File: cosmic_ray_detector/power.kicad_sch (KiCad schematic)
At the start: 16 parts

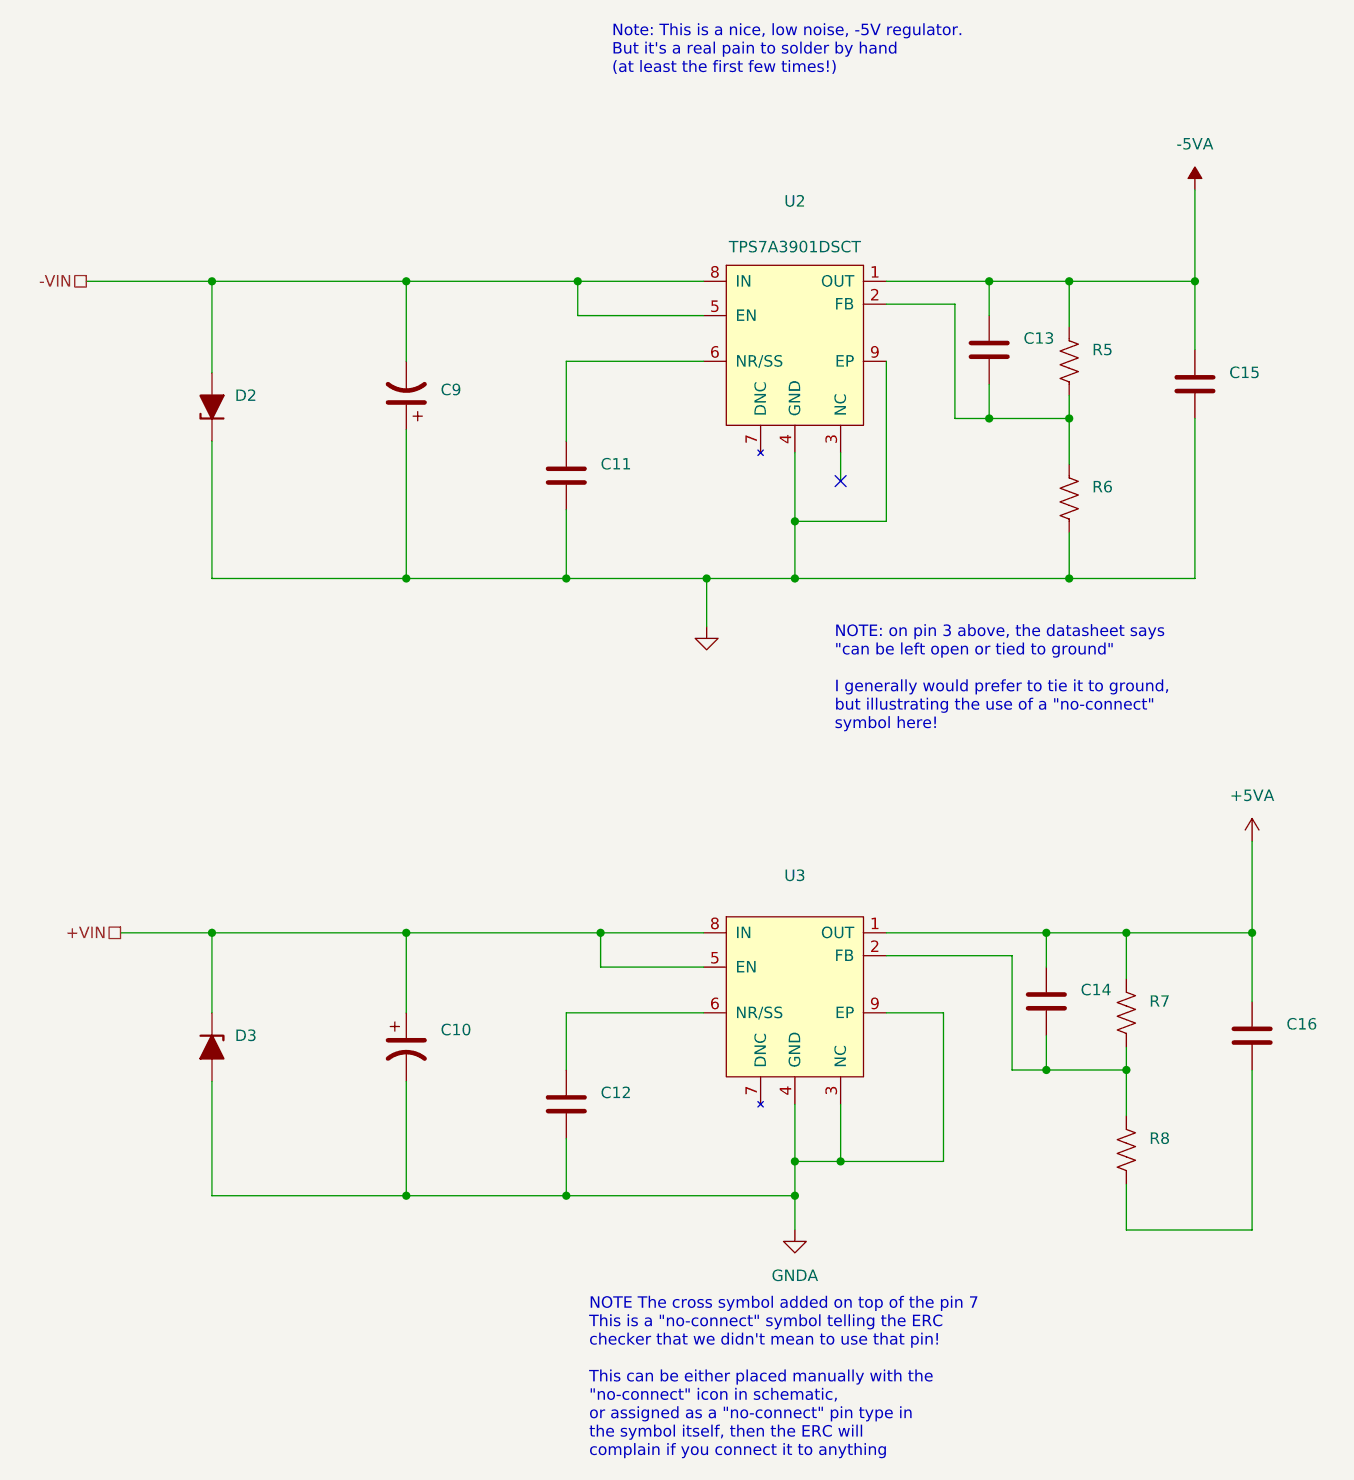
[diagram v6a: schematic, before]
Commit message: add conceptual design, tweaks to schematics
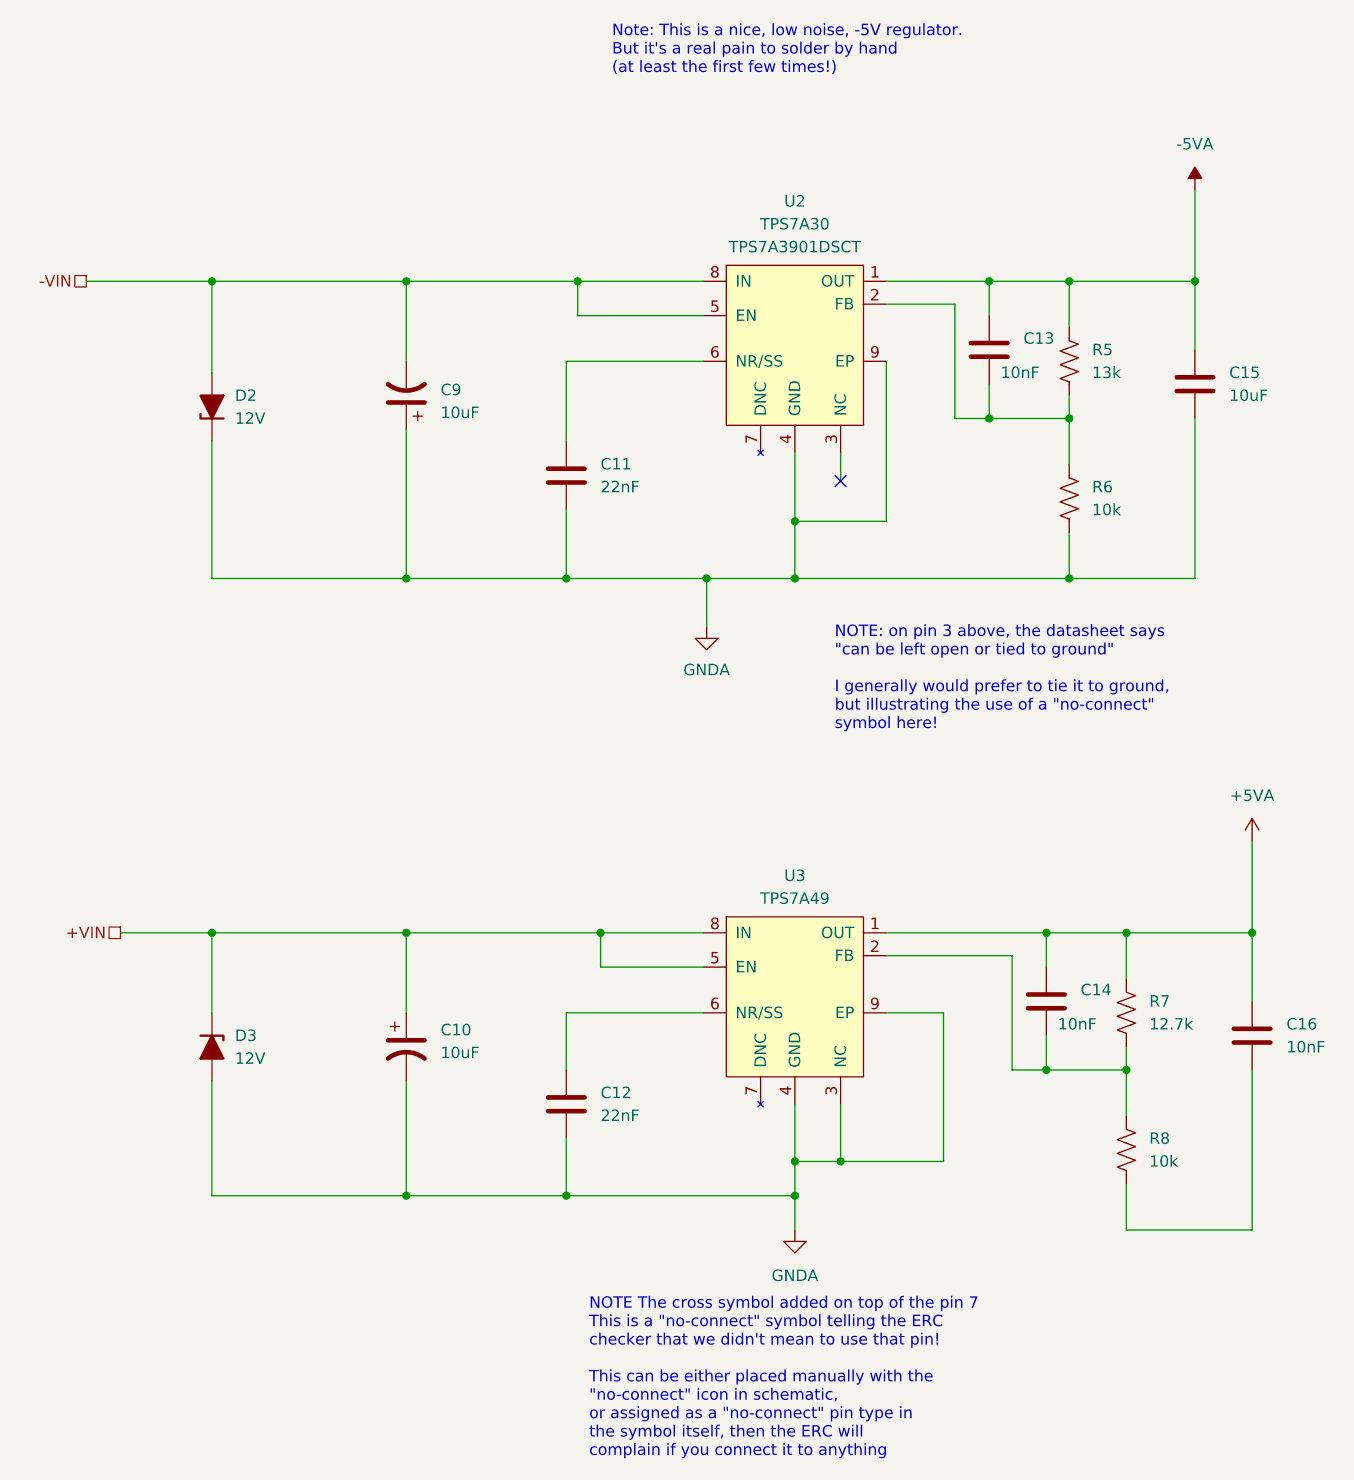
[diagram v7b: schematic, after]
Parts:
- C10, C15, C9: value (none) -> 10uF; footprint (none) -> cosmic_ray_detector_lib:MAL215375109E3
- C11, C12: value (none) -> 22nF; footprint (none) -> Capacitor_SMD:C_0402_1005Metric
- C13, C14, C16: value (none) -> 10nF; footprint (none) -> Capacitor_SMD:C_0402_1005Metric
- D2, D3: value (none) -> 12V; footprint (none) -> Diode_SMD:D_SOD-123
- R5: value (none) -> 13k; footprint (none) -> Resistor_SMD:R_0402_1005Metric
- R6, R8: value (none) -> 10k; footprint (none) -> Resistor_SMD:R_0402_1005Metric
- R7: value (none) -> 12.7k; footprint (none) -> Resistor_SMD:R_0402_1005Metric
- U2: value (none) -> TPS7A30; footprint (none) -> cosmic_ray_detector_lib:MSOP-8-1EP_3x3mm_P0.65mm_EP1.73x1.85mm_ThermalVias
- U3: value (none) -> TPS7A49; footprint (none) -> cosmic_ray_detector_lib:MSOP-8-1EP_3x3mm_P0.65mm_EP1.73x1.85mm_ThermalVias
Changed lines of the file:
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@@
       (effects (font (size 1.27 1.27)) (justify left))
     )
-    (property "Value" "" (id 1) (at 165.1 149.8599 0)
-      (effects (font (size 1.27 1.27)) (justify left))
-    )
-    (property "Footprint" "" (id 2) (at 163.576 148.844 90)
+    (property "Value" "10k" (id 1) (at 165.1 149.8599 0)
+      (effects (font (size 1.27 1.27)) (justify left))
+    )
+    (property "Footprint" "Resistor_SMD:R_0402_1005Metric" (id 2) (at 163.576 148.844 90)
       (effects (font (size 1.27 1.27)) hide)
     )
@@
       (effects (font (size 1.27 1.27)) (justify left))
     )
-    (property "Value" "" (id 1) (at 165.1 134.6199 0)
-      (effects (font (size 1.27 1.27)) (justify left))
-    )
-    (property "Footprint" "" (id 2) (at 163.576 133.604 90)
+    (property "Value" "12.7k" (id 1) (at 165.1 134.6199 0)
+      (effects (font (size 1.27 1.27)) (justify left))
+    )
+    (property "Footprint" "Resistor_SMD:R_0402_1005Metric" (id 2) (at 163.576 133.604 90)
       (effects (font (size 1.27 1.27)) hide)
     )
@@
       (effects (font (size 1.27 1.27)) (justify left))
     )
-    (property "Value" "" (id 1) (at 86.36 137.7949 0)
-      (effects (font (size 1.27 1.27)) (justify left))
-    )
-    (property "Footprint" "" (id 2) (at 82.55 137.16 0)
+    (property "Value" "10uF" (id 1) (at 86.36 137.7949 0)
+      (effects (font (size 1.27 1.27)) (justify left))
+    )
+    (property "Footprint" "cosmic_ray_detector_lib:MAL215375109E3" (id 2) (at 82.55 137.16 0)
       (effects (font (size 1.27 1.27)) hide)
     )
@@
       (effects (font (size 1.27 1.27)) (justify left))
     )
-    (property "Value" "" (id 1) (at 180.34 137.1599 0)
-      (effects (font (size 1.27 1.27)) (justify left))
-    )
-    (property "Footprint" "" (id 2) (at 177.4952 139.7 0)
+    (property "Value" "10nF" (id 1) (at 180.34 137.1599 0)
+      (effects (font (size 1.27 1.27)) (justify left))
+    )
+    (property "Footprint" "Capacitor_SMD:C_0402_1005Metric" (id 2) (at 177.4952 139.7 0)
       (effects (font (size 1.27 1.27)) hide)
     )
@@
       (effects (font (size 1.27 1.27)) (justify left))
     )
-    (property "Value" "" (id 1) (at 158.75 62.2299 0)
-      (effects (font (size 1.27 1.27)) (justify left))
-    )
-    (property "Footprint" "" (id 2) (at 157.226 61.214 90)
+    (property "Value" "13k" (id 1) (at 158.75 62.2299 0)
+      (effects (font (size 1.27 1.27)) (justify left))
+    )
+    (property "Footprint" "Resistor_SMD:R_0402_1005Metric" (id 2) (at 157.226 61.214 90)
       (effects (font (size 1.27 1.27)) hide)
     )
@@
       (effects (font (size 1.27 1.27)) hide)
     )
-    (property "Value" "" (id 1) (at 115.9256 95.25 0))
+    (property "Value" "GNDA" (id 1) (at 115.9256 95.25 0))
     (property "Footprint" "" (id 2) (at 115.9256 90.4748 0)
       (effects (font (size 1.27 1.27)) hide)
@@
       (effects (font (size 1.27 1.27)) (justify left))
     )
-    (property "Value" "" (id 1) (at 158.75 77.4699 0)
-      (effects (font (size 1.27 1.27)) (justify left))
-    )
-    (property "Footprint" "" (id 2) (at 157.226 76.454 90)
+    (property "Value" "10k" (id 1) (at 158.75 77.4699 0)
+      (effects (font (size 1.27 1.27)) (justify left))
+    )
+    (property "Footprint" "Resistor_SMD:R_0402_1005Metric" (id 2) (at 157.226 76.454 90)
       (effects (font (size 1.27 1.27)) hide)
     )
@@
       (effects (font (size 1.27 1.27)) (justify left))
     )
-    (property "Value" "" (id 1) (at 154.94 134.62 0)
-      (effects (font (size 1.27 1.27)) (justify left))
-    )
-    (property "Footprint" "" (id 2) (at 154.6352 135.89 0)
+    (property "Value" "10nF" (id 1) (at 154.94 134.62 0)
+      (effects (font (size 1.27 1.27)) (justify left))
+    )
+    (property "Footprint" "Capacitor_SMD:C_0402_1005Metric" (id 2) (at 154.6352 135.89 0)
       (effects (font (size 1.27 1.27)) hide)
     )
@@
       (effects (font (size 1.27 1.27)) (justify left))
     )
-    (property "Value" "" (id 1) (at 104.14 74.9299 0)
-      (effects (font (size 1.27 1.27)) (justify left))
-    )
-    (property "Footprint" "" (id 2) (at 101.2952 77.47 0)
+    (property "Value" "22nF" (id 1) (at 104.14 74.9299 0)
+      (effects (font (size 1.27 1.27)) (justify left))
+    )
+    (property "Footprint" "Capacitor_SMD:C_0402_1005Metric" (id 2) (at 101.2952 77.47 0)
       (effects (font (size 1.27 1.27)) hide)
     )
@@
       (effects (font (size 1.27 1.27)) (justify left))
     )
-    (property "Value" "" (id 1) (at 63.5 138.4299 90)
-      (effects (font (size 1.27 1.27)) (justify left))
-    )
-    (property "Footprint" "" (id 2) (at 60.96 137.16 0)
+    (property "Value" "12V" (id 1) (at 63.5 138.4299 90)
+      (effects (font (size 1.27 1.27)) (justify left))
+    )
+    (property "Footprint" "Diode_SMD:D_SOD-123" (id 2) (at 60.96 137.16 0)
       (effects (font (size 1.27 1.27)) hide)
     )
@@
     (in_bom yes) (on_board yes) (fields_autoplaced)
     (property "Reference" "U2" (id 0) (at 125.73 43.18 0))
-    (property "Value" "" (id 1) (at 125.73 45.72 0))
-    (property "Footprint" "" (id 2) (at 125.73 54.61 0)
+    (property "Value" "TPS7A30" (id 1) (at 125.73 45.72 0))
+    (property "Footprint" "cosmic_ray_detector_lib:MSOP-8-1EP_3x3mm_P0.65mm_EP1.73x1.85mm_ThermalVias" (id 2) (at 125.73 54.61 0)
       (effects (font (size 1.27 1.27)) hide)
     )
@@
       (effects (font (size 1.27 1.27)) (justify left))
     )
-    (property "Value" "" (id 1) (at 173.99 64.7699 0)
-      (effects (font (size 1.27 1.27)) (justify left))
-    )
-    (property "Footprint" "" (id 2) (at 171.1452 67.31 0)
+    (property "Value" "10uF" (id 1) (at 173.99 64.7699 0)
+      (effects (font (size 1.27 1.27)) (justify left))
+    )
+    (property "Footprint" "cosmic_ray_detector_lib:MAL215375109E3" (id 2) (at 171.1452 67.31 0)
       (effects (font (size 1.27 1.27)) hide)
     )
@@
     (in_bom yes) (on_board yes) (fields_autoplaced)
     (property "Reference" "U3" (id 0) (at 125.73 118.11 0))
-    (property "Value" "" (id 1) (at 125.73 120.65 0))
-    (property "Footprint" "" (id 2) (at 125.73 127 0)
+    (property "Value" "TPS7A49" (id 1) (at 125.73 120.65 0))
+    (property "Footprint" "cosmic_ray_detector_lib:MSOP-8-1EP_3x3mm_P0.65mm_EP1.73x1.85mm_ThermalVias" (id 2) (at 125.73 127 0)
       (effects (font (size 1.27 1.27)) hide)
     )
@@
       (effects (font (size 1.27 1.27)) (justify left))
     )
-    (property "Value" "" (id 1) (at 104.14 144.7799 0)
-      (effects (font (size 1.27 1.27)) (justify left))
-    )
-    (property "Footprint" "" (id 2) (at 101.2952 147.32 0)
+    (property "Value" "22nF" (id 1) (at 104.14 144.7799 0)
+      (effects (font (size 1.27 1.27)) (justify left))
+    )
+    (property "Footprint" "Capacitor_SMD:C_0402_1005Metric" (id 2) (at 101.2952 147.32 0)
       (effects (font (size 1.27 1.27)) hide)
     )
@@
       (effects (font (size 1.27 1.27)) (justify right))
     )
-    (property "Value" "" (id 1) (at 63.5 67.3099 90)
+    (property "Value" "12V" (id 1) (at 63.5 67.3099 90)
       (effects (font (size 1.27 1.27)) (justify right))
     )
-    (property "Footprint" "" (id 2) (at 60.96 66.04 0)
+    (property "Footprint" "Diode_SMD:D_SOD-123" (id 2) (at 60.96 66.04 0)
       (effects (font (size 1.27 1.27)) hide)
     )
@@
       (effects (font (size 1.27 1.27)) (justify left))
     )
-    (property "Value" "" (id 1) (at 148.59 62.23 0)
-      (effects (font (size 1.27 1.27)) (justify left))
-    )
-    (property "Footprint" "" (id 2) (at 148.2852 63.5 0)
+    (property "Value" "10nF" (id 1) (at 148.59 62.23 0)
+      (effects (font (size 1.27 1.27)) (justify left))
+    )
+    (property "Footprint" "Capacitor_SMD:C_0402_1005Metric" (id 2) (at 148.2852 63.5 0)
       (effects (font (size 1.27 1.27)) hide)
     )
@@
       (effects (font (size 1.27 1.27)) (justify right))
     )
-    (property "Value" "" (id 1) (at 86.36 66.6749 0)
+    (property "Value" "10uF" (id 1) (at 86.36 66.6749 0)
       (effects (font (size 1.27 1.27)) (justify right))
     )
-    (property "Footprint" "" (id 2) (at 82.55 64.77 0)
-      (effects (font (size 1.27 1.27)) hide)
-    )
+    (property "Footprint" "cosmic_ray_detector_lib:MAL215375109E3" (id 2) (at 82.55 64.77 0)
+      (effects (font (size 1.27 1.27)) hide)
+    )

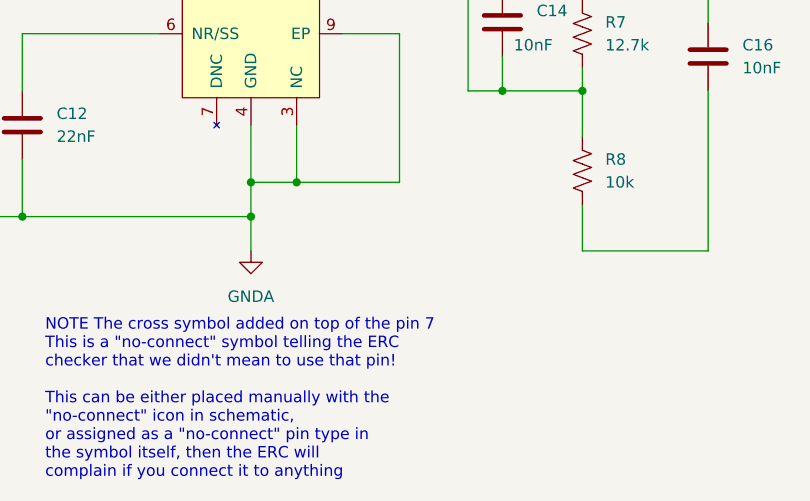
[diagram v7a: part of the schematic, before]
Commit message: label demos and add netclasses to schematic
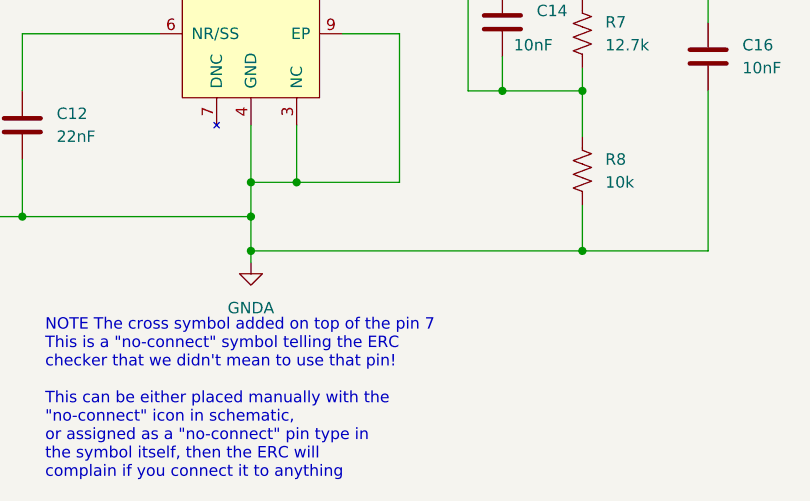
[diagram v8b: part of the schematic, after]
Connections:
- net GNDA: now also C16.2, R8.2
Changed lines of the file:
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@@
   (junction (at 162.56 139.7) (diameter 0) (color 0 0 0 0)
+  )
+  (junction (at 162.56 157.48) (diameter 0) (color 0 0 0 0)
+  )
+  (junction (at 125.73 157.48) (diameter 0) (color 0 0 0 0)
   )
   (junction (at 82.55 52.07) (diameter 0) (color 0 0 0 0)
@@
     (stroke (width 0) (type default) (color 0 0 0 0))
   )
+  (wire (pts (xy 125.73 157.48) (xy 162.56 157.48))
+    (stroke (width 0) (type default) (color 0 0 0 0))
+  )
   (wire (pts (xy 101.6 55.88) (xy 101.6 52.07))
     (stroke (width 0) (type default) (color 0 0 0 0))
   )
   (wire (pts (xy 60.96 153.67) (xy 82.55 153.67))
+    (stroke (width 0) (type default) (color 0 0 0 0))
+  )
+  (wire (pts (xy 125.73 157.48) (xy 125.73 158.75))
     (stroke (width 0) (type default) (color 0 0 0 0))
   )
@@
     (pin "2")
   )
-  (symbol (lib_id "power:GNDA") (at 125.73 157.48 0) (unit 1)
-    (in_bom yes) (on_board yes) (fields_autoplaced)
-    (property "Reference" "#PWR013" (id 0) (at 125.73 163.83 0)
-      (effects (font (size 1.27 1.27)) hide)
-    )
-    (property "Value" "GNDA" (id 1) (at 125.73 162.56 0))
-    (property "Footprint" "" (id 2) (at 125.73 157.48 0)
-      (effects (font (size 1.27 1.27)) hide)
-    )
-    (property "Datasheet" "" (id 3) (at 125.73 157.48 0)
-      (effects (font (size 1.27 1.27)) hide)
-    )
+  (symbol (lib_id "power:GNDA") (at 125.73 158.75 0) (unit 1)
+    (in_bom yes) (on_board yes) (fields_autoplaced)
+    (property "Reference" "#PWR013" (id 0) (at 125.73 165.1 0)
+      (effects (font (size 1.27 1.27)) hide)
+    )
+    (property "Value" "GNDA" (id 1) (at 125.73 163.83 0))
+    (property "Footprint" "" (id 2) (at 125.73 158.75 0)
+      (effects (font (size 1.27 1.27)) hide)
+    )
+    (property "Datasheet" "" (id 3) (at 125.73 158.75 0)
+      (effects (font (size 1.27 1.27)) hide)
+    )
